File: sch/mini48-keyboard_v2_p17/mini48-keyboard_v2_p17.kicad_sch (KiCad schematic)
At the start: 1 part

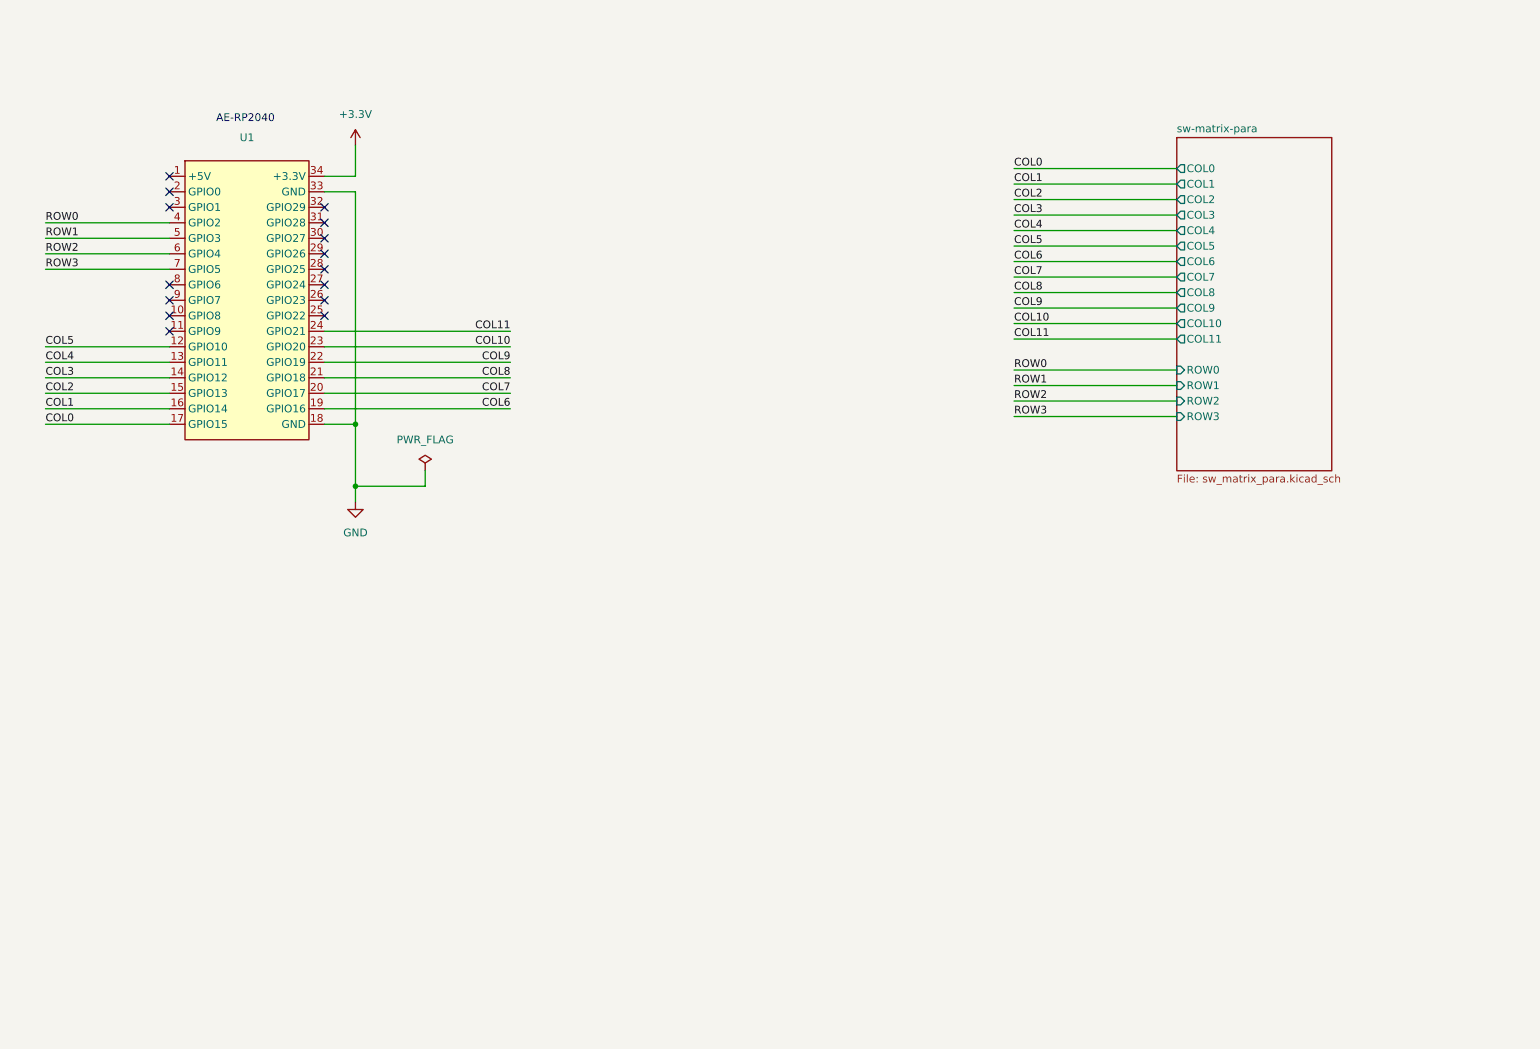
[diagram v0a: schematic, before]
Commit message: ざっくり配線しました。 pico と  ae-rp2040 を選択できるようにしました。
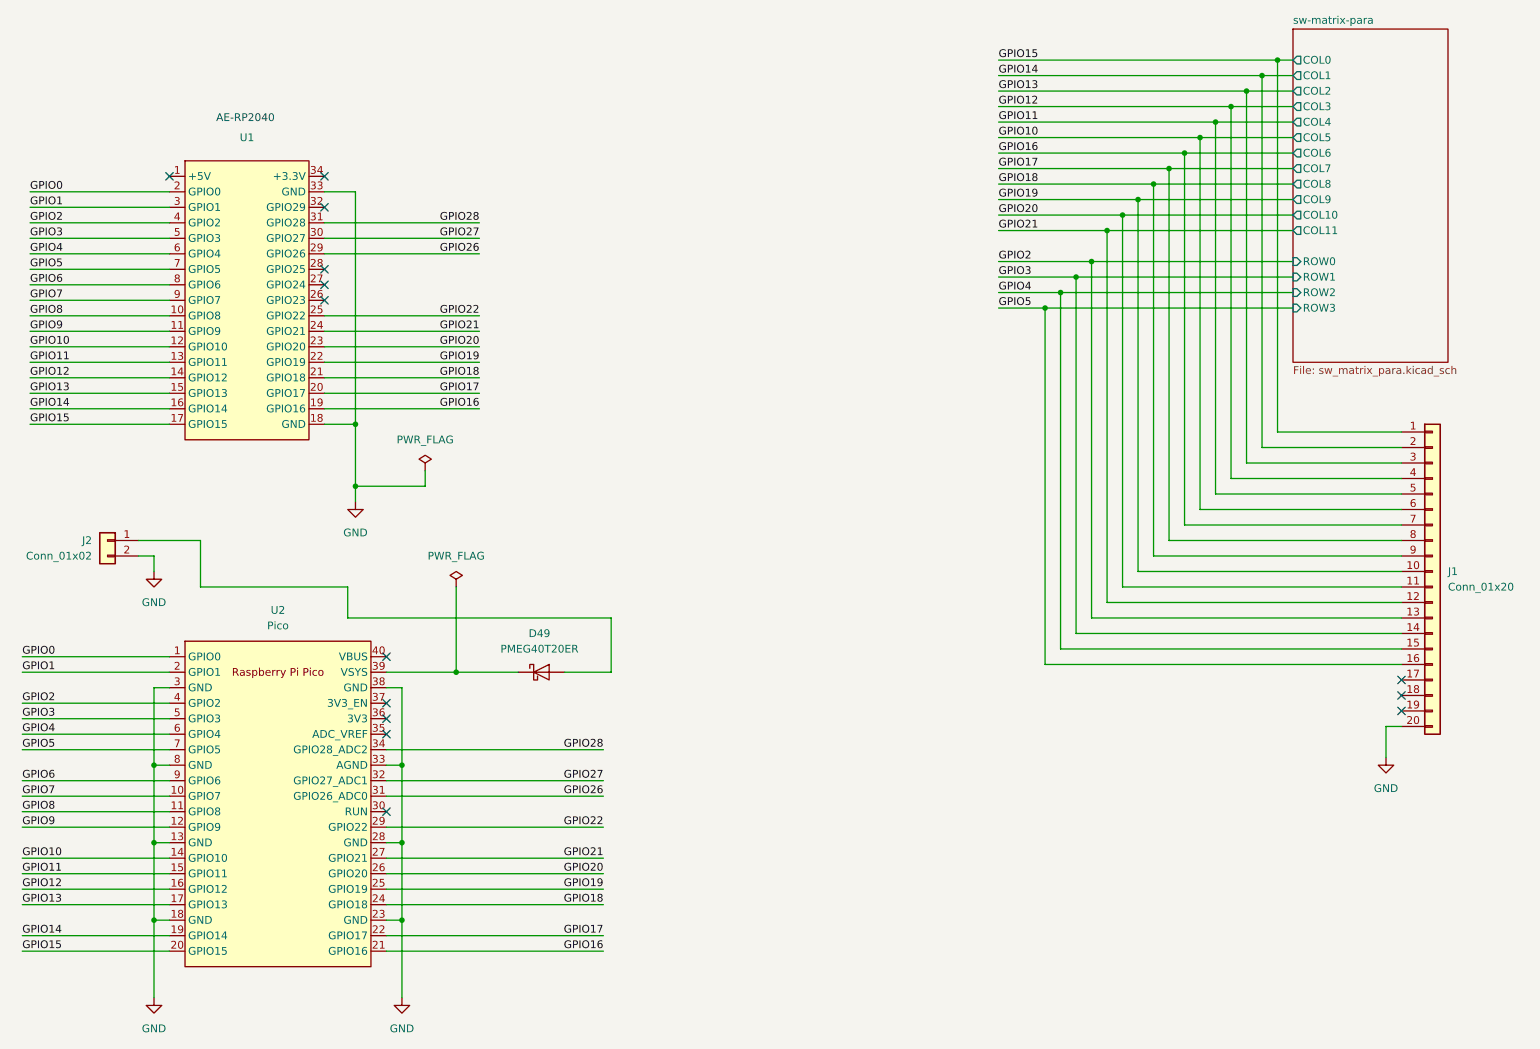
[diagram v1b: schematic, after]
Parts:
- added D49: PMEG40T20ER, Diode_SMD:Nexperia_CFP3_SOD-123W, symbol Diode:PMEG40T20ER
- added J1: Conn_01x20, Connector_PinHeader_2.54mm:PinHeader_1x20_P2.54mm_Vertical, symbol Connector_Generic:Conn_01x20
- added J2: Conn_01x02, Connector_JST:JST_PH_B2B-PH-K_1x02_P2.00mm_Vertical, symbol Connector_Generic:Conn_01x02
- added U2: Pico, my_pico:pico_no_dbg_smd_th_p0.85, symbol my_pico:my_pico_no_dbg
- U1: footprint ae-rp2040:AE-RP2040 -> ae-rp2040:AE-RP2040_p0.85
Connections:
- net GND: now also J1.20 (Pin_20), J2.2 (Pin_2), U2.13 (GND), U2.18 (GND), U2.23 (GND), U2.28 (GND), U2.3 (GND), U2.33 (AGND), U2.38 (GND), U2.8 (GND)
- net GPIO8: now reaches U1.10 (GPIO8)
- net GPIO8: now also U2.11 (GPIO8)
- net GPIO9: now reaches U1.11 (GPIO9)
- net GPIO9: now also U2.12 (GPIO9)
- net GPIO0: now reaches U1.2 (GPIO0)
- net GPIO0: now also U2.1 (GPIO0)
- net GPIO22: now reaches U1.25 (GPIO22)
- net GPIO22: now also U2.29 (GPIO22)
- net GPIO26: now reaches U1.29 (GPIO26)
- net GPIO26: now also U2.31 (GPIO26_ADC0)
- net GPIO1: now reaches U1.3 (GPIO1)
- net GPIO1: now also U2.2 (GPIO1)
- net GPIO27: now reaches U1.30 (GPIO27)
- net GPIO27: now also U2.32 (GPIO27_ADC1)
- net GPIO28: now reaches U1.31 (GPIO28)
- net GPIO28: now also U2.34 (GPIO28_ADC2)
- net GPIO6: now reaches U1.8 (GPIO6)
- net GPIO6: now also U2.9 (GPIO6)
- net GPIO7: now reaches U1.9 (GPIO7)
- net GPIO7: now also U2.10 (GPIO7)
- net +3.3V: no longer names the net of U1.34 (+3.3V)
- net COL0 renamed GPIO15
- net GPIO15: now also J1.1 (Pin_1), U2.20 (GPIO15)
- net COL1 renamed GPIO14
- net GPIO14: now also J1.2 (Pin_2), U2.19 (GPIO14)
- net COL10 renamed GPIO20
- net GPIO20: now also J1.11 (Pin_11), U2.26 (GPIO20)
- net COL11 renamed GPIO21
- net GPIO21: now also J1.12 (Pin_12), U2.27 (GPIO21)
- net COL2 renamed GPIO13
- net GPIO13: now also J1.3 (Pin_3), U2.17 (GPIO13)
- net COL3 renamed GPIO12
- net GPIO12: now also J1.4 (Pin_4), U2.16 (GPIO12)
- net COL4 renamed GPIO11
- net GPIO11: now also J1.5 (Pin_5), U2.15 (GPIO11)
- net COL5 renamed GPIO10
- net GPIO10: now also J1.6 (Pin_6), U2.14 (GPIO10)
- net COL6 renamed GPIO16
- net GPIO16: now also J1.7 (Pin_7), U2.21 (GPIO16)
- net COL7 renamed GPIO17
- net GPIO17: now also J1.8 (Pin_8), U2.22 (GPIO17)
- net COL8 renamed GPIO18
- net GPIO18: now also J1.9 (Pin_9), U2.24 (GPIO18)
- net COL9 renamed GPIO19
- net GPIO19: now also J1.10 (Pin_10), U2.25 (GPIO19)
- net ROW0 renamed GPIO2
- net GPIO2: now also J1.13 (Pin_13), U2.4 (GPIO2)
- net ROW1 renamed GPIO3
- net GPIO3: now also J1.14 (Pin_14), U2.5 (GPIO3)
- net ROW2 renamed GPIO4
- net GPIO4: now also J1.15 (Pin_15), U2.6 (GPIO4)
- net ROW3 renamed GPIO5
- net GPIO5: now also J1.16 (Pin_16), U2.7 (GPIO5)
- new net: D49.1 (K), U2.39 (VSYS)
- new net: D49.2 (A), J2.1 (Pin_1)
- no-connect marks 15 -> 14

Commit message: LCDのクロック線周りを微修正。
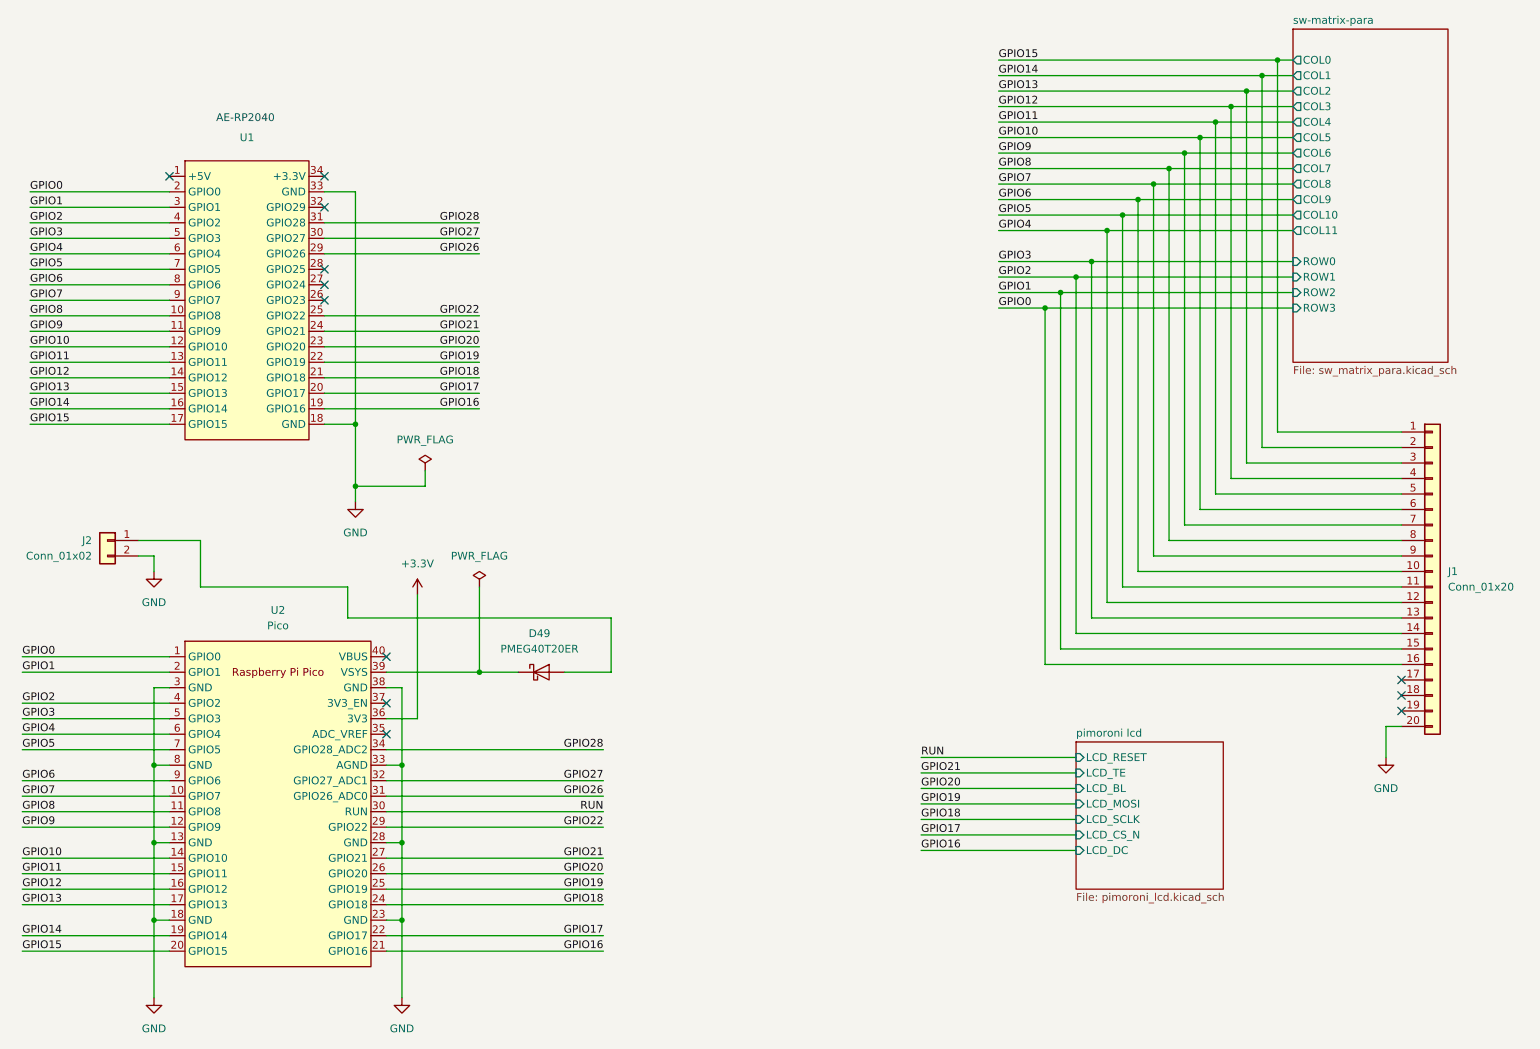
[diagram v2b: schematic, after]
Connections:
- net GPIO0: now also J1.16 (Pin_16)
- net GPIO1: now also J1.15 (Pin_15)
- net GPIO16: no longer J1.7 (Pin_7)
- net GPIO17: no longer J1.8 (Pin_8)
- net GPIO18: no longer J1.9 (Pin_9)
- net GPIO19: no longer J1.10 (Pin_10)
- net GPIO2: now also J1.14 (Pin_14); no longer J1.13 (Pin_13)
- net GPIO20: no longer J1.11 (Pin_11)
- net GPIO21: no longer J1.12 (Pin_12)
- net GPIO3: now also J1.13 (Pin_13); no longer J1.14 (Pin_14)
- net GPIO4: now also J1.12 (Pin_12); no longer J1.15 (Pin_15)
- net GPIO5: now also J1.11 (Pin_11); no longer J1.16 (Pin_16)
- net GPIO6: now also J1.10 (Pin_10)
- net GPIO7: now also J1.9 (Pin_9)
- net GPIO8: now also J1.8 (Pin_8)
- net GPIO9: now also J1.7 (Pin_7)
- net RUN: now reaches U2.30 (RUN)
- net +3.3V: now reaches U2.36 (3V3)
- no-connect marks 14 -> 12
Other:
- added sheet pimoroni lcd (pimoroni_lcd.kicad_sch)

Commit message: マイコンボードを pico のみに変更しました。 スイッチのシートの名前を変えました。
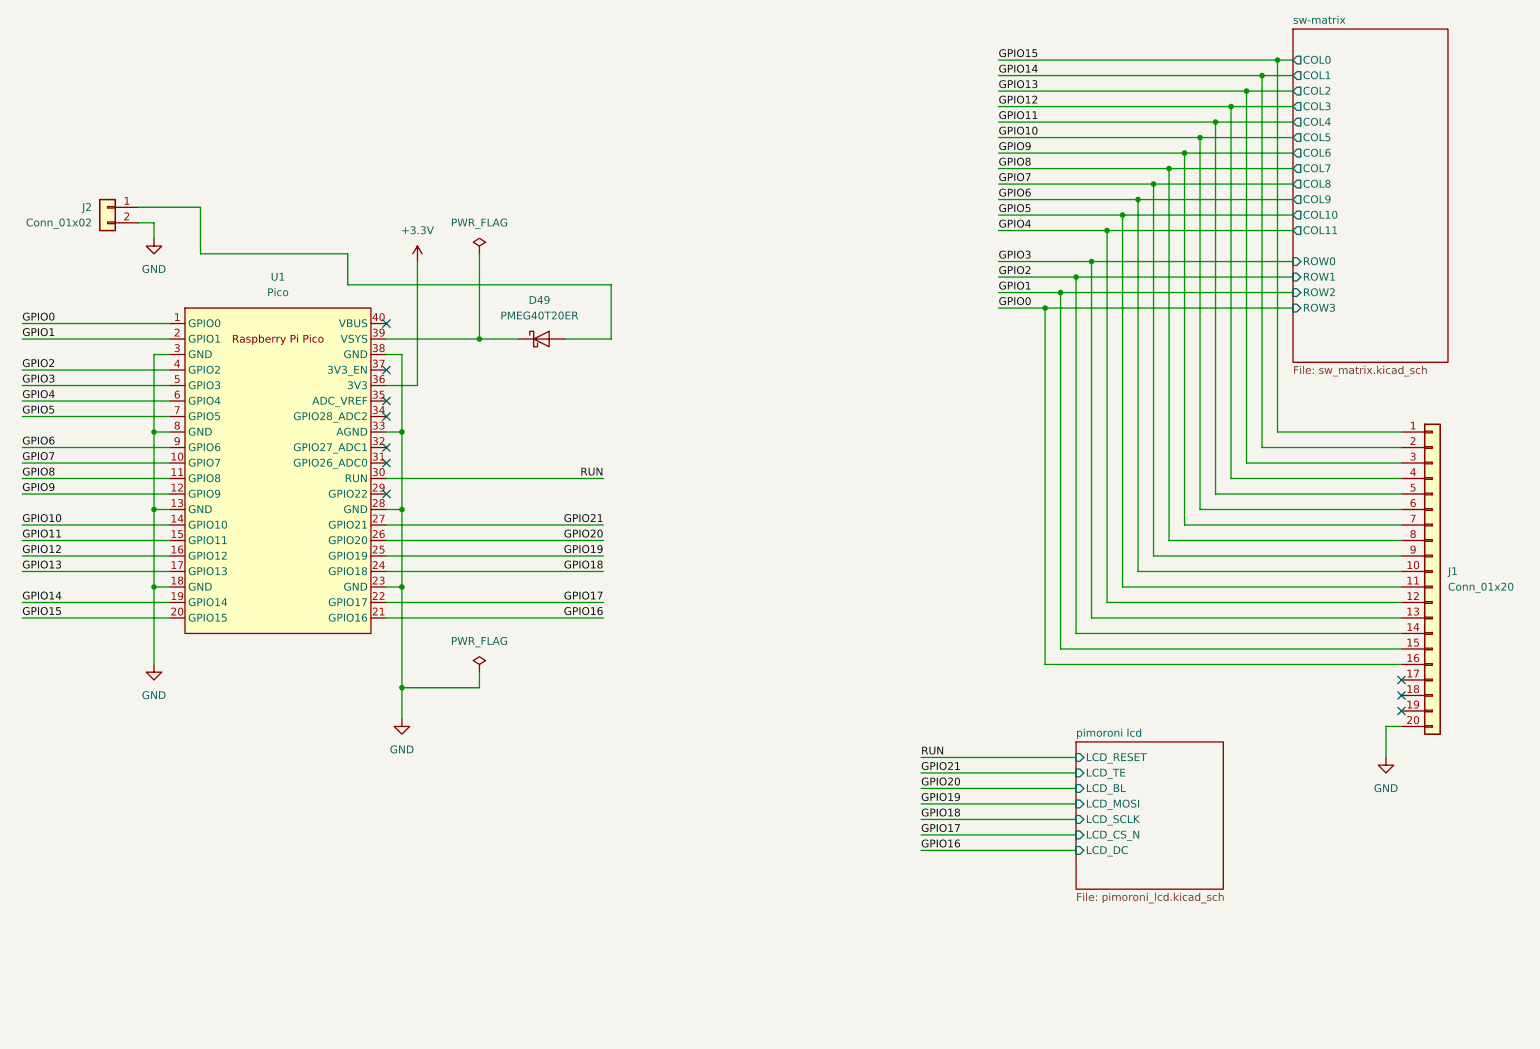
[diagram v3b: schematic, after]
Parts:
- removed U1: ~, ae-rp2040:AE-RP2040_p0.85, symbol ae-rp2040:AE-RP2040
- renumbered U2 to U1
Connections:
- net GPIO22: no longer names the net of U1.29 (GPIO22)
- net GPIO26: no longer names the net of U1.31 (GPIO26_ADC0)
- net GPIO27: no longer names the net of U1.32 (GPIO27_ADC1)
- net GPIO28: no longer names the net of U1.34 (GPIO28_ADC2)
- no-connect marks 12 -> 10
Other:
- sheet sw-matrix-para renamed sw-matrix
- sheet sw-matrix: file sw_matrix_para.kicad_sch -> sw_matrix.kicad_sch
- note removed: "AE-RP2040"
- moved on the sheet: D49, J2, U1
